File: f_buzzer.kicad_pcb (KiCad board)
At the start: 2 copper layers, 71.5 x 44 mm, 11 parts, among them U1 SN74123N

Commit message: First SMD revision
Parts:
- C1, C2: footprint Capacitor_THT:C_Disc_D5.1mm_W3.2mm_P5.00mm -> Capacitor_SMD:C_0603_1608Metric
- C3: value C -> 7n; footprint Capacitor_THT:C_Disc_D5.1mm_W3.2mm_P5.00mm -> Capacitor_SMD:C_0603_1608Metric
- R1, R2, R3: footprint Resistor_THT:R_Axial_DIN0207_L6.3mm_D2.5mm_P7.62mm_Horizontal -> Resistor_SMD:R_0603_1608Metric
- U1: value SN74123N -> SN74LS123DRG4; footprint Package_DIP:DIP-16_W7.62mm -> f_buzzer:SN74LS123DRG4
- moved C2 20.3 mm to (132.8, 82.9), turned to 90 degrees
- moved R2 19.4 mm to (130.2, 79.6), turned to 0 degrees
- moved C3 13.8 mm to (132.7, 90.2), turned to 180 degrees
- moved R1 12.8 mm to (132.6, 86.4), turned to 0 degrees
- moved R3 12.5 mm to (121.9, 80.4), turned to 90 degrees
- moved C1 10.9 mm to (121.8, 88.4), turned to 270 degrees
- moved U1 10.0 mm to (126.9, 85.8), turned to 0 degrees
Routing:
- net Net-(BZ1-Pad1): track 93.6 -> 71.3 mm
- net Net-(R1-Pad1): track 24.6 -> 8.94 mm
- net Net-(C2-Pad1): track 17.9 -> 3.46 mm
- net Net-(C2-Pad2): track 16.1 -> 6.81 mm
- net Net-(C1-Pad2): track 18.8 -> 11.7 mm
- net Net-(U1-Pad10): track 10.8 -> 6.53 mm
- net Net-(C1-Pad1): track 6.11 -> 2.62 mm
- net VCC: track 69.9 -> 66.7 mm
- net Net-(C3-Pad1): track 24.4 -> 22.9 mm
- net /DVR: track 68.3 -> 68.8 mm
- removed copper zone on B.Cu, net GND
- removed copper zone on F.Cu, net GND

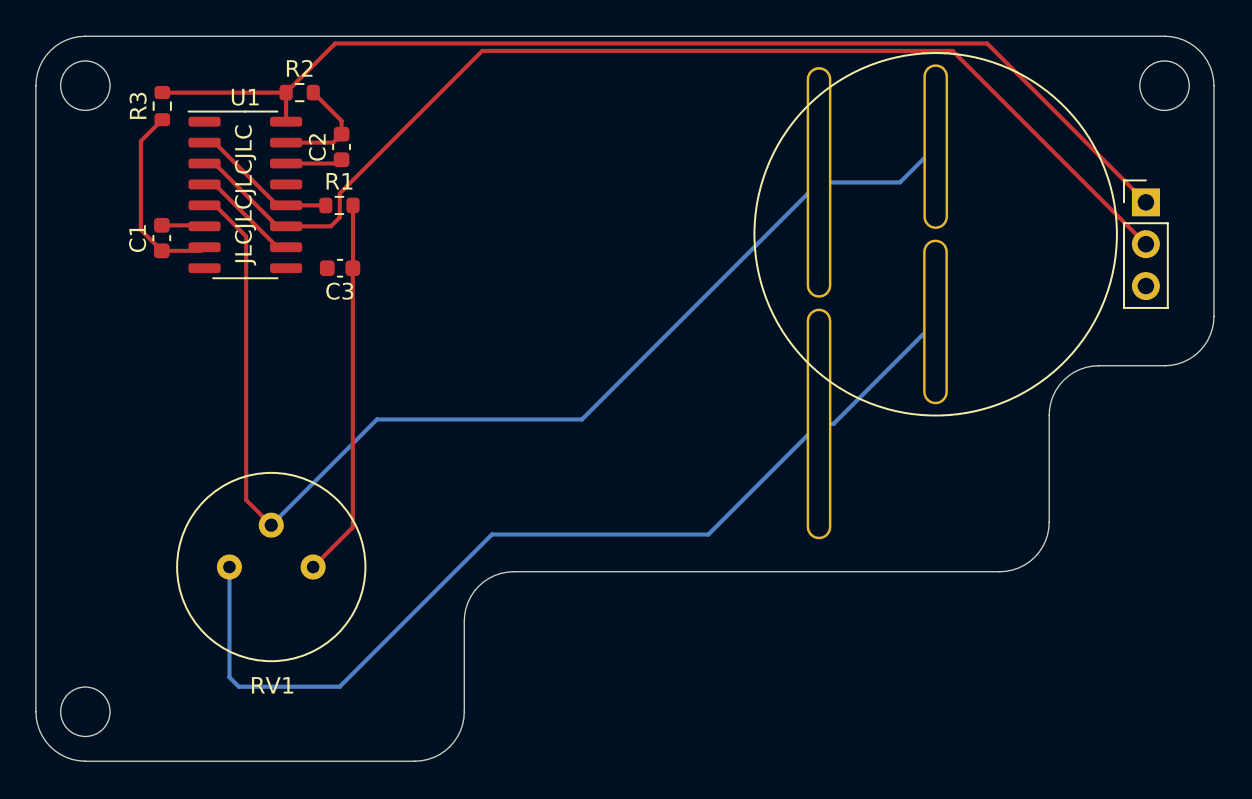
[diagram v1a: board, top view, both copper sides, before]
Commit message: Added fill zones
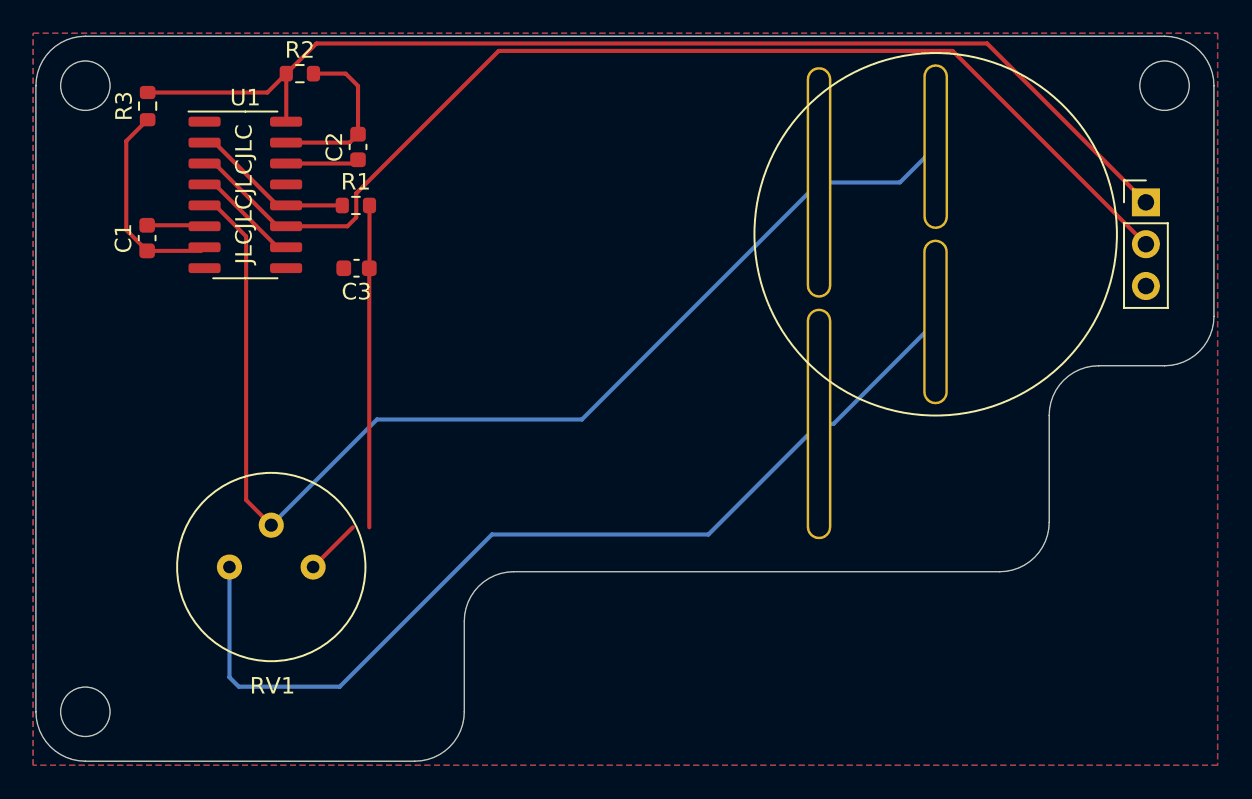
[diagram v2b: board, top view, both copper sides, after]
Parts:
- moved R2 1.15 mm to (130.2, 78.4)
- moved C2 1.00 mm to (133.8, 82.9)
- moved C3 1.00 mm to (133.7, 90.2)
- moved R1 1.00 mm to (133.6, 86.4)
- moved C1 0.89 mm to (121.0, 88.4)
- moved R3 0.89 mm to (121.0, 80.4)
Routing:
- net Net-(C2-Pad2): track 6.81 -> 10.5 mm
- net VCC: track 66.7 -> 68.8 mm
- net Net-(R1-Pad1): track 8.94 -> 9.94 mm
- net Net-(C2-Pad1): track 3.46 -> 4.46 mm
- net Net-(C1-Pad2): track 11.7 -> 12.6 mm
- net Net-(C1-Pad1): track 2.62 -> 3.51 mm
- added copper zone on B.Cu, net GND
- added copper zone on F.Cu, net GND

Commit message: Updated the buzzer footprints
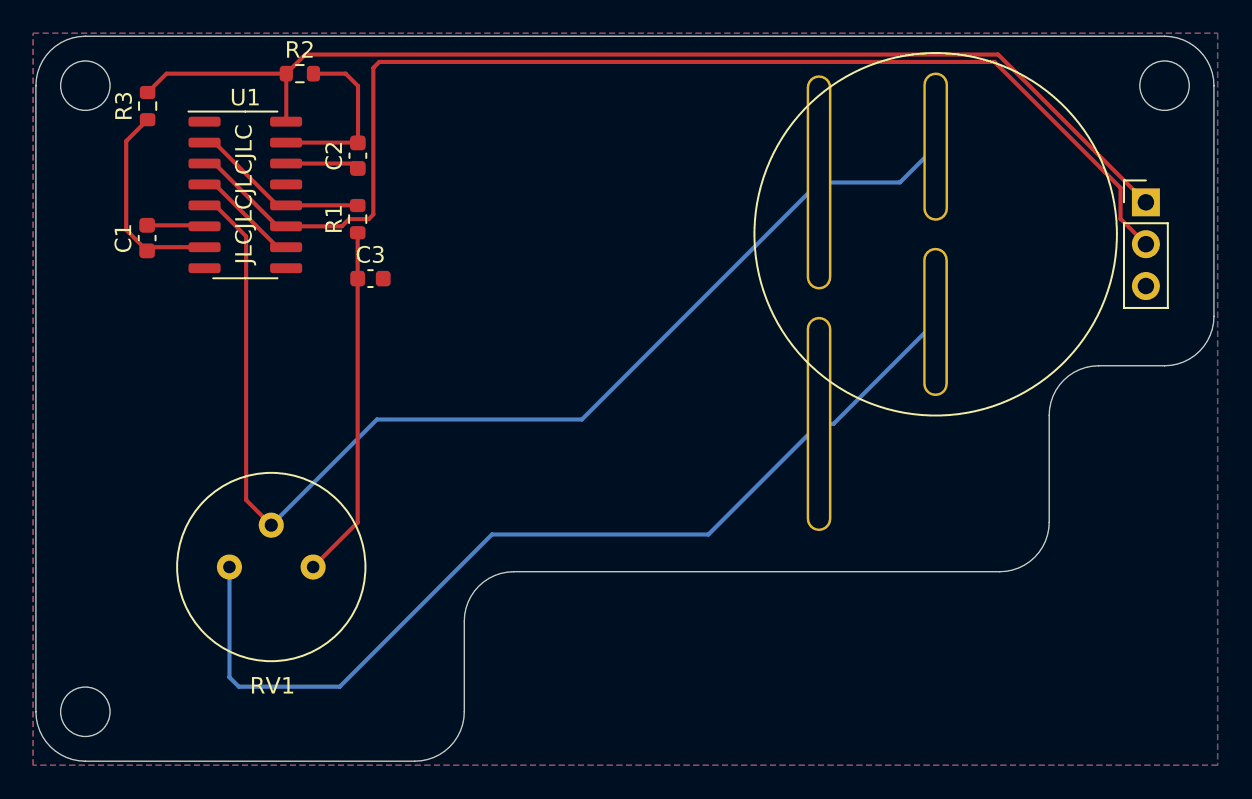
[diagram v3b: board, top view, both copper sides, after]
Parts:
- moved C3 1.05 mm to (134.5, 90.9), turned to 0 degrees
- moved R1 0.84 mm to (133.7, 87.2), turned to 270 degrees
- moved C2 0.53 mm to (133.8, 83.4)
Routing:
- net /DVR: track 68.8 -> 73.7 mm
- net Net-(C3-Pad1): track 22.9 -> 21.4 mm
- net Net-(R1-Pad1): track 9.94 -> 10.9 mm
- net VCC: track 68.8 -> 68.2 mm

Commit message: Updated the SN74LS123DRG4 footprint
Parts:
- U1: footprint f_buzzer:SN74LS123DRG4 -> Package_SO:SOIC-16_3.9x9.9mm_P1.27mm

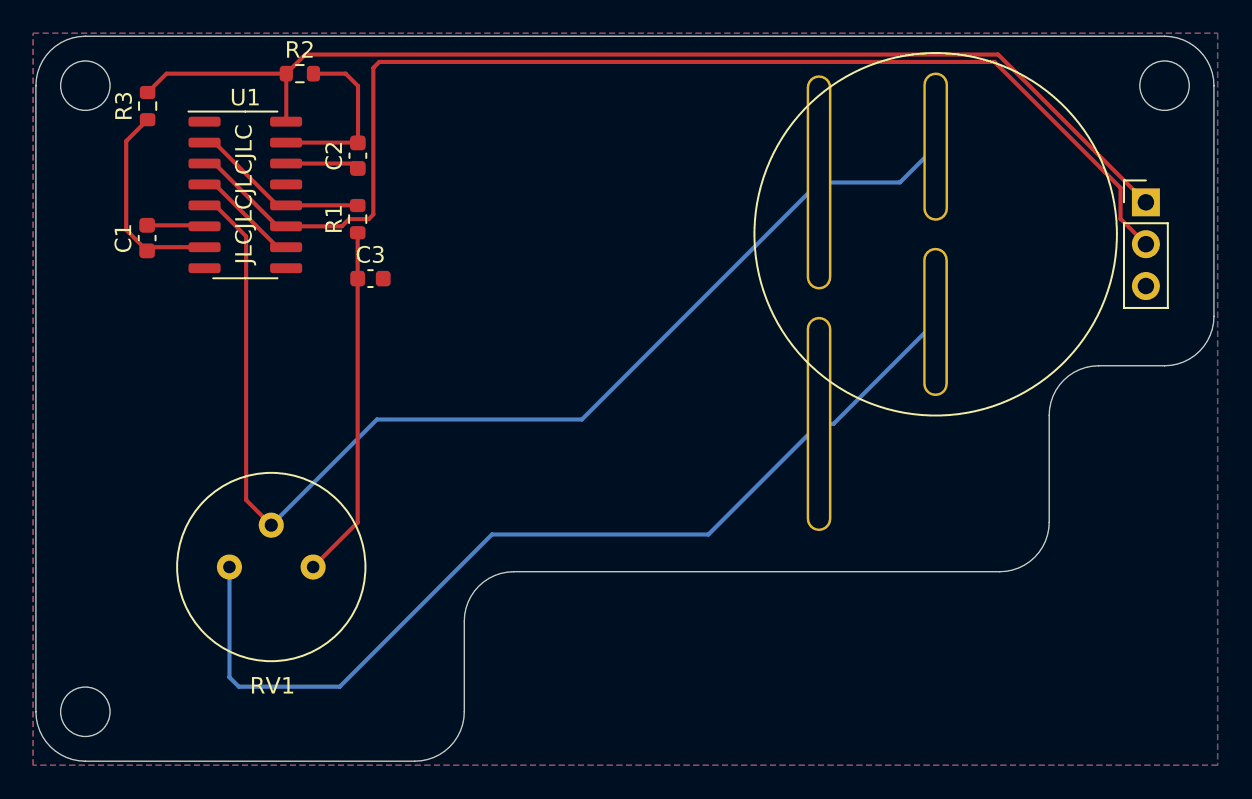
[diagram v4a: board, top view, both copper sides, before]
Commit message: Updated the schematics and pcb design
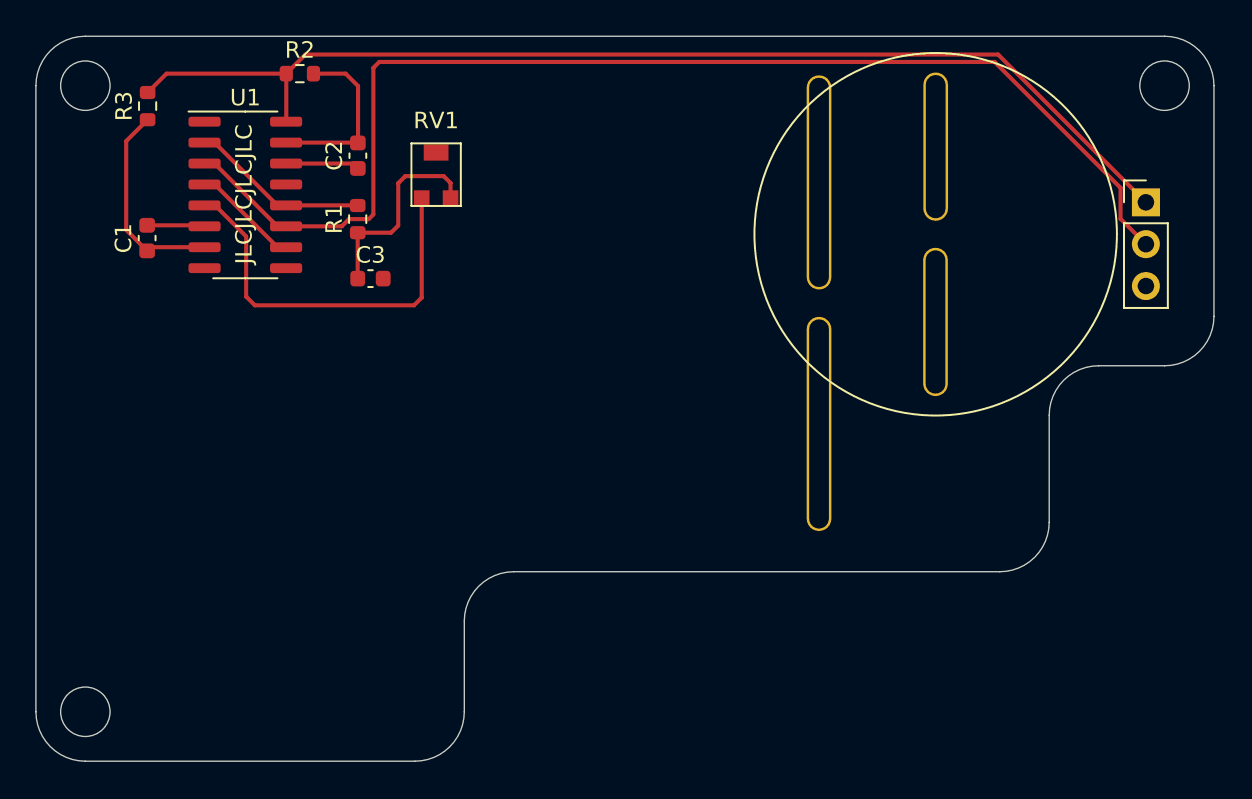
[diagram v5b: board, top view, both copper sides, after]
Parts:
- RV1: footprint f_buzzer:Potentiometer_Bourns_3345P_Horizontal -> f_buzzer:VG039NCHXTB203
- moved RV1 25.9 mm to (138.5, 84.5)
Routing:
- net Net-(BZ1-Pad2): track 59.0 -> 0.00 mm
- net Net-(BZ1-Pad1): track 71.3 -> 24.1 mm
- net Net-(C3-Pad1): track 21.4 -> 12.4 mm
- removed copper zone on B.Cu, net GND
- removed copper zone on F.Cu, net GND
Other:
- board text removed: "No components should be located inside the circle (except for the potentiometer). The surface of the disc is visible from the cutout of the back case of the IBM 4704 series keyboard."
- board text removed: "No components should be placed inside the cercle. This where the IBM 4704 series keyboard feet attaches to the back case."
- board text removed: "These areas are to be avoided for placing components or pads."
